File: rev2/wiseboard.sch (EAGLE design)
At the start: 75 parts, among them IC2 LM358MX, Q1 IRLML6402TRPBF, Q2 IRLML6402TRPBF, U1 LT1945EMSPBF, U2 BQ24210DQCT, U3 ESP-WROOM-03

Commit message: Connect flash chip, battery voltage, solar cell voltage
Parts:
- removed C16, C9: 2u2F, resistor:C-USC0805
- removed JP4: JUMPER, Sparkfun-Passives:JUMPER-SMT_2_NC_PASTE_NO-SILK
- removed Q2: IRLML6402TRPBF, IRLML6402:IRLML6402TRPBF
- removed R28: 10k, resistor:R-US_R0805
- removed R29: 33k, resistor:R-US_R0805
- added C10: 10uF, resistor:C-USC0805
- added R15, R17, R18: 10K, resistor:R-US_R0805
- R1: value 12k -> 10K
- R16: value 100k -> 10k
- R2: value 47k -> 10k
- renumbered R35 to R16
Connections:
- removed net 15V: U$4.VPOS
- removed net BOOSTENA: R2.1
- removed net CHARGE_EN: JP4.2, U2.!EN
- removed net N$12: R28.2
- removed net N$13: C9.1, D1.C, U2.VBUS
- removed net N$24: U3.TXD
- removed net N$25: U3.RXD
- removed net N$26: R16.1, S3.P, S3.P1, S4.P, S4.P1, S5.P, S5.P1, S6.P, S6.P1, S7.P, S7.P1
- removed net N$3: Q1.G, R1.2, R2.2
- removed net N$32: U3.IO0
- removed net N$44: U3.IO26
- removed net N$50: U3.SENSOR_VP
- removed net N$51: U3.SENSOR_VN
- removed net N$7: D1.A, SOLAR.2, SOLARPIN.2
- removed net VDD: Q2.D
- new net BAT_SENS: R1.1, R15.2, U3.SENSOR_VP
- new net CLK: U$23.CLK, U3.SCK
- new net CS: U$23.CS, U3.SCS
- new net DPAD: R16.1, S3.P, S3.P1, S4.P, S4.P1, S5.P, S5.P1, S6.P, S6.P1, S7.P, S7.P1, U3.IO0
- new net ESP_DI: U$23.DO, U3.SDI
- new net ESP_DO: U$23.DI, U3.SDO
- new net PANEL: C8.2, D1.A, D1.C, R17.2, SOLAR.2, SOLARPIN.2, U2.VBUS
- new net PANEL_SENS: R17.1, R18.2, U3.SENSOR_VN
- new net SUP_CTRL: Q1.G, R2.2, U3.IO26
- net +15V: now also U$4.VPOS
- net +3V3: now also U3.3V3, U3.EN; no longer C16.1, Q2.S
- net GND: now also C10.1, C8.1, R15.1, R18.1, U2.!EN; no longer C16.2, C8.2, C9.2, JP4.1
- net RXD: now also U3.RXD
- net TXD: now also U3.TXD
- net VBAT: now also C10.2, R1.2, R2.1; no longer C8.1, R1.1
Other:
- note added: "Check to see if these are need."
- moved on the sheet: C8, R1, R2

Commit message: first run through of ERC
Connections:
- removed net N$41: U3.IO21
- new net N$3: C8.2, D1.C, U2.VBUS
- net PANEL: no longer C8.2, D1.C, U2.VBUS
- net SPH: now also U3.IO21
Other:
- note added: "Screen Connector"
- note removed: "Check to see if these are need."
- note removed: "Shift Registers and Screen Connector"
- moved on the sheet: BAT_CON, BAT_PIN, C10, C8, CHRG/LBO, D1, D2, DONE, POWERGOOD, R1, R10, R13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

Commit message: Semi-Final Schematic
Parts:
- removed R16, R32: 10k, resistor:R-US_R0805
- removed R30: 1K, resistor:R-US_R0805
- removed R31: 2k, resistor:R-US_R0805
- removed R33: 12k, resistor:R-US_R0805
- removed R34: 33k, resistor:R-US_R0805
- removed S1, S2, S3, S4, S5, S6, S7: (no value), switch-omron:10-XX
- removed U$23: W25Q32JVSSIQ, WISE:W25Q32JVSSIQ
- added IC5: W25Q, WISE:W25Q32JVSSIQ
- added SW1, SW2: SPST_TACT-KMR2, adafruit:SPST_TACT-KMR2
- IC1: value LT1945EMSPBF -> LT1945
- IC2: value LM358MX -> LM358
- IC3: value 497-7303-1-ND -> L79L15
- IC4: value 497-7278-1-ND -> L78L15
- renumbered U$2 to IC4, U$3 to IC3, U1 to IC1
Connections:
- removed net CS: U$23.CS, U3.SCS
- removed net DPAD: R16.1, S3.P, S3.P1, S4.P, S4.P1, S5.P, S5.P1, S6.P, S6.P1, S7.P, S7.P1, U3.IO0
- removed net N$27: R30.1, S3.S, S3.S1
- removed net N$29: R31.1, S4.S, S4.S1
- removed net N$31: R32.1, S5.S, S5.S1
- removed net N$33: R33.1, S6.S, S6.S1
- removed net N$35: R34.1, S7.S, S7.S1
- new net IC5: IC5.CS, U3.SCS
- new net N$7: U3.IO0
- net +3V3: now also IC5.VCC, IC5.WP; no longer R30.2, R31.2, R32.2, R33.2, R34.2, U$23.VCC, U$23.WP
- net -20V: now also IC3.VIN@3, IC3.VIN@6, IC3.VIN@7
- net CLK: now also IC5.CLK; no longer U$23.CLK
- net ESP_DI: now also IC5.DO; no longer U$23.DO
- net ESP_DO: now also IC5.DI; no longer U$23.DI
- net GND: now also IC5.GND, SW1.P, SW1.P1, SW2.P, SW2.P1; no longer R16.2, S1.P, S1.P1, S2.P, S2.P1, U$23.GND
- net GPIO0: now also SW1.S, SW1.S1; no longer S1.S, S1.S1
- net RESET: now also SW2.S, SW2.S1; no longer S2.S, S2.S1
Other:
- note removed: "Button Array and Battery Monitor"
- moved on the sheet: C7, D2, D3, IC2A, JP1, R22, R9, VR1

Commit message: Add edge connectors to lbr, Prelim PCB layout, Consolidation, Fix mistakes
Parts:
- removed BAT_CON: (no value), adafruit:JST_2PIN-SMT-RA
- removed BAT_PIN, SOLARPIN: (no value), pinhead:PINHD-1X2
- removed C7: 100nF, resistor:C-USC0805
- removed JP1: PROG_HEADER, pinhead:PINHD-1X4
- removed R11, R12: 10k, resistor:R-US_R0805
- removed SOLAR: 455-1749-1-ND, adafruit:JST_2PIN-SMT-RA
- added J1: BAT_CON, WISE:EDGE_CON_22PIN
- added J2: SOL_CON, WISE:EDGE_CON_22PIN
- added J3: PROG_HEADER, WISE:EDGE_CON_4
- BOOT: value GREEN -> LED1
- C1, C3, C6: value 100nF -> 1uF
- C2: value 2u2F -> 1uF
- C4: value 100pF -> 10uF
- C5: value 4.7pF -> 10uF
- CHRG/LBO: value ORANGE -> LED3
- DONE: value GREEN -> LED4
- IC8: value AP2112K-3.3TRG1DICT-ND -> IC6
- POWERGOOD: value BLUE -> LED2
- Q1: value IRLML6402TRPBF -> IRLM
- R4, R7: value 33k -> 39k
- renumbered U$14 to IC8, U$6 to D4, U$7 to D5, U$8 to D6, U2 to IC9
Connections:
- net +15V: no longer IC2P.V+
- net -15V: no longer IC2P.V-
- net GND: now also J1.1, J2.1, J3.4; no longer BAT_CON.1, BAT_PIN.2, C7.2, JP1.4, R11.1, R12.1, SOLAR.1, SOLARPIN.1
- net NEGEN: no longer R11.2
- net PANEL: now also J2.2; no longer SOLAR.2, SOLARPIN.2
- net POSEN: no longer R12.2
- net RXD_5V: now also J3.2; no longer JP1.2
- net TXD: now also J3.1; no longer JP1.1
- net VBAT: now also J1.2; no longer BAT_CON.2, BAT_PIN.1
- net VCC: now also J3.3; no longer JP1.3
- net VCOMMON: no longer C7.1

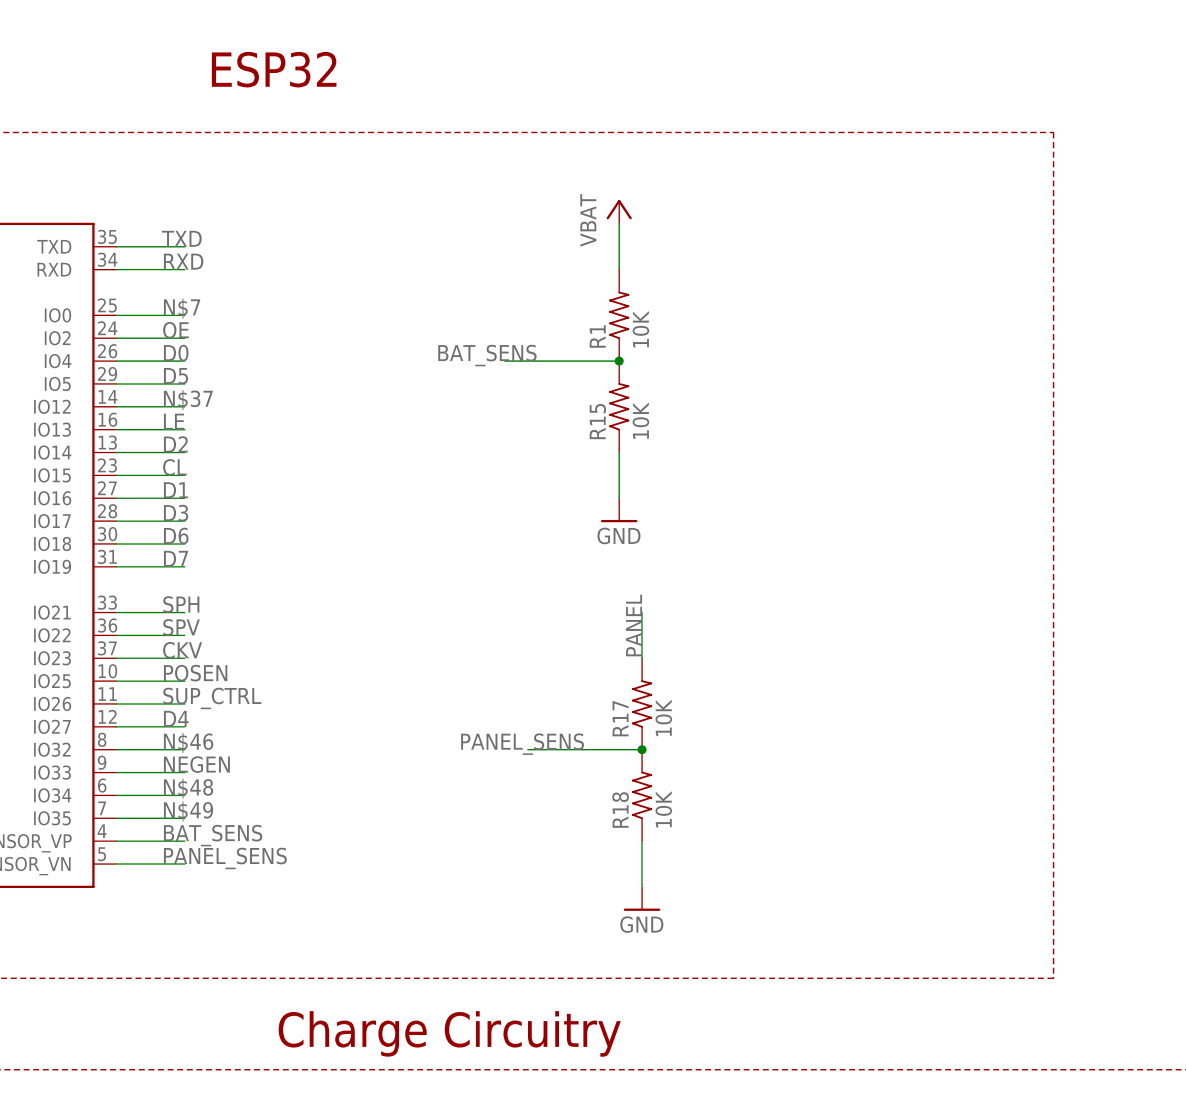
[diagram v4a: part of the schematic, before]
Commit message: Add button header, 2nd revision of pcb layout, mess up a bunch of save files
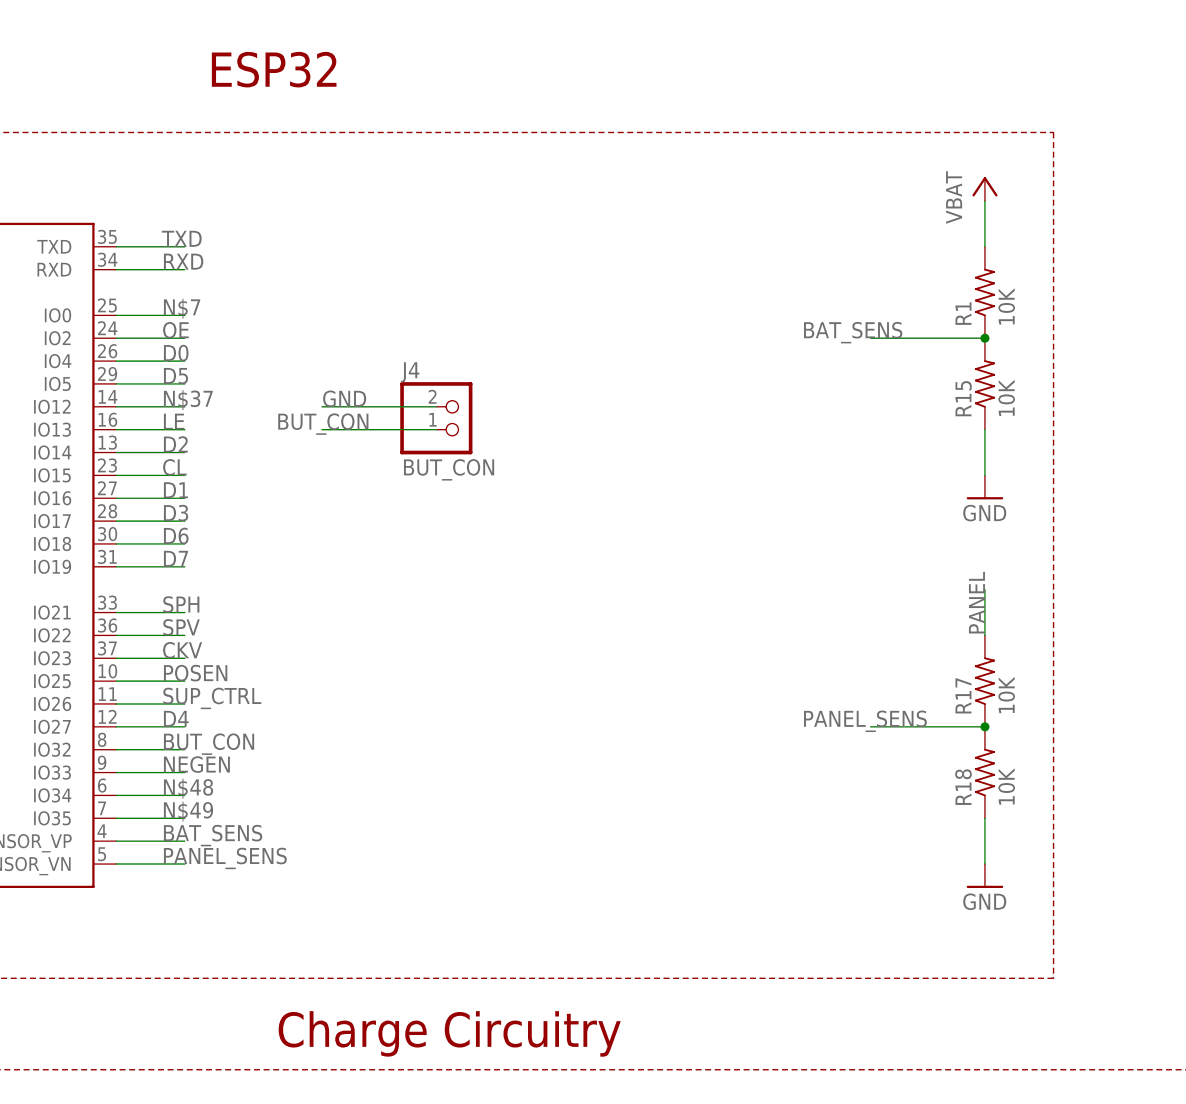
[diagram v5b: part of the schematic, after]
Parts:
- added J4: BUT_CON, WISE:EDGE_CON_22PIN
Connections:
- removed net N$46: U3.IO32
- new net BUT_CON: J4.2, U3.IO32
- net GND: now also J4.1
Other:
- moved on the sheet: R1, R15, R17, R18
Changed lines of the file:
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@@
 <part name="J2" library="WISE" deviceset="EDGE_CON_2" device="2PIN" value="SOL_CON"/>
 <part name="J3" library="WISE" deviceset="EDGE_CON_4" device="" value="PROG_HEADER"/>
+<part name="J4" library="WISE" deviceset="EDGE_CON_2" device="2PIN" value="BUT_CON"/>
 </parts>
 <sheets>
@@
 <instance part="R2" gate="G$1" x="-365.76" y="-33.02" rot="R270"/>
 <instance part="+3V3" gate="G$1" x="93.98" y="12.7" rot="R90"/>
-<instance part="R1" gate="G$1" x="195.58" y="7.62" rot="R90"/>
-<instance part="R15" gate="G$1" x="195.58" y="-2.54" rot="R90"/>
-<instance part="U$1" gate="G$1" x="195.58" y="20.32"/>
-<instance part="GND24" gate="1" x="195.58" y="-15.24"/>
+<instance part="R1" gate="G$1" x="236.22" y="10.16" rot="R90"/>
+<instance part="R15" gate="G$1" x="236.22" y="0" rot="R90"/>
+<instance part="U$1" gate="G$1" x="236.22" y="22.86"/>
+<instance part="GND24" gate="1" x="236.22" y="-12.7"/>
 <instance part="C10" gate="G$1" x="236.22" y="-106.68"/>
 <instance part="GND27" gate="1" x="236.22" y="-99.06" rot="R180"/>
 <instance part="C8" gate="G$1" x="132.08" y="-96.52"/>
-<instance part="R17" gate="G$1" x="198.12" y="-35.56" rot="R90"/>
-<instance part="R18" gate="G$1" x="198.12" y="-45.72" rot="R90"/>
-<instance part="GND28" gate="1" x="198.12" y="-58.42"/>
+<instance part="R17" gate="G$1" x="236.22" y="-33.02" rot="R90"/>
+<instance part="R18" gate="G$1" x="236.22" y="-43.18" rot="R90"/>
+<instance part="GND28" gate="1" x="236.22" y="-55.88"/>
 <instance part="SW1" gate="G$1" x="-2.54" y="55.88"/>
 <instance part="SW2" gate="G$1" x="17.78" y="55.88"/>
@@
 <instance part="J2" gate="G$1" x="93.98" y="-111.76" rot="R180"/>
 <instance part="J3" gate="G$1" x="162.56" y="73.66" rot="R180"/>
+<instance part="J4" gate="G$1" x="177.8" y="-2.54"/>
 </instances>
 <busses>
@@
 <pinref part="R15" gate="G$1" pin="1"/>
 <pinref part="GND24" gate="1" pin="GND"/>
-<wire x1="195.58" y1="-12.7" x2="195.58" y2="-7.62" width="0.1524" layer="91"/>
+<wire x1="236.22" y1="-10.16" x2="236.22" y2="-5.08" width="0.1524" layer="91"/>
 </segment>
 <segment>
@@
 <pinref part="R18" gate="G$1" pin="1"/>
 <pinref part="GND28" gate="1" pin="GND"/>
-<wire x1="198.12" y1="-55.88" x2="198.12" y2="-50.8" width="0.1524" layer="91"/>
+<wire x1="236.22" y1="-53.34" x2="236.22" y2="-48.26" width="0.1524" layer="91"/>
+</segment>
+<segment>
+<pinref part="J4" gate="G$1" pin="1"/>
+<wire x1="175.26" y1="-2.54" x2="162.56" y2="-2.54" width="0.1524" layer="91"/>
+<label x="162.56" y="-2.54" size="1.778" layer="95"/>
 </segment>
 </net>
@@
 <segment>
 <pinref part="R17" gate="G$1" pin="2"/>
-<wire x1="198.12" y1="-25.4" x2="198.12" y2="-30.48" width="0.1524" layer="91"/>
-<label x="198.12" y="-30.48" size="1.778" layer="95" rot="R90"/>
+<wire x1="236.22" y1="-22.86" x2="236.22" y2="-27.94" width="0.1524" layer="91"/>
+<label x="236.22" y="-27.94" size="1.778" layer="95" rot="R90"/>
 </segment>
 </net>
@@
 <pinref part="R1" gate="G$1" pin="2"/>
 <pinref part="U$1" gate="G$1" pin="VBAT"/>
-<wire x1="195.58" y1="17.78" x2="195.58" y2="12.7" width="0.1524" layer="91"/>
+<wire x1="236.22" y1="20.32" x2="236.22" y2="15.24" width="0.1524" layer="91"/>
 </segment>
 <segment>
@@
 </segment>
 </net>
-<net name="N$46" class="0">
+<net name="BUT_CON" class="0">
 <segment>
 <pinref part="U3" gate="G$1" pin="IO32"/>
@@
 <label x="144.78" y="-40.64" size="1.778" layer="95"/>
 </segment>
+<segment>
+<pinref part="J4" gate="G$1" pin="2"/>
+<wire x1="175.26" y1="-5.08" x2="162.56" y2="-5.08" width="0.1524" layer="91"/>
+<label x="157.48" y="-5.08" size="1.778" layer="95"/>
+</segment>
 </net>
 <net name="N$48" class="0">
@@
 <net name="BAT_SENS" class="0">
 <segment>
-<wire x1="182.88" y1="2.54" x2="195.58" y2="2.54" width="0.1524" layer="91"/>
+<wire x1="223.52" y1="5.08" x2="236.22" y2="5.08" width="0.1524" layer="91"/>
 <pinref part="R1" gate="G$1" pin="1"/>
 <pinref part="R15" gate="G$1" pin="2"/>
-<junction x="195.58" y="2.54"/>
-<label x="175.26" y="2.54" size="1.778" layer="95"/>
+<junction x="236.22" y="5.08"/>
+<label x="215.9" y="5.08" size="1.778" layer="95"/>
 </segment>
 <segment>
@@
 </segment>
 <segment>
-<wire x1="185.42" y1="-40.64" x2="198.12" y2="-40.64" width="0.1524" layer="91"/>
+<wire x1="223.52" y1="-38.1" x2="236.22" y2="-38.1" width="0.1524" layer="91"/>
 <pinref part="R17" gate="G$1" pin="1"/>
 <pinref part="R18" gate="G$1" pin="2"/>
-<junction x="198.12" y="-40.64"/>
-<label x="177.8" y="-40.64" size="1.778" layer="95"/>
-</segment>
-</net>
+<junction x="236.22" y="-38.1"/>
+<label x="215.9" y="-38.1" size="1.778" layer="95"/>
+</segment>
+</net>

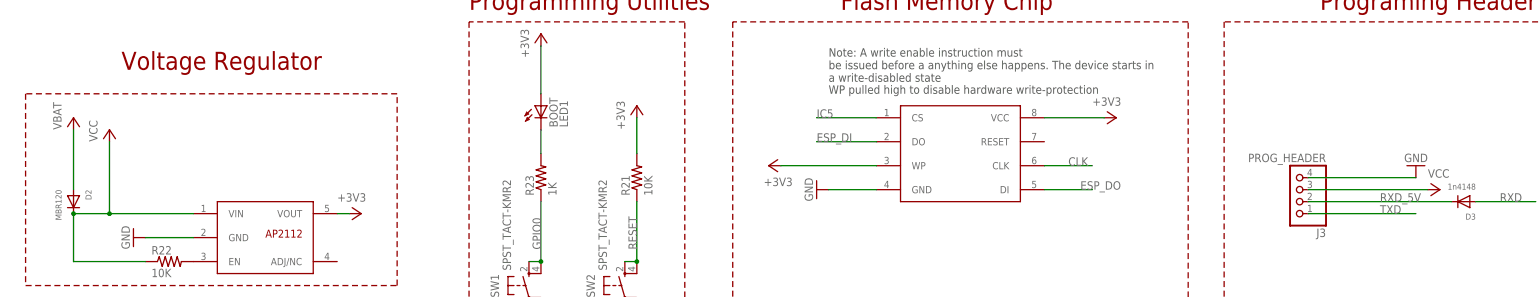
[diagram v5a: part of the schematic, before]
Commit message: fix file troubles, semi finalize layout, fix component labels
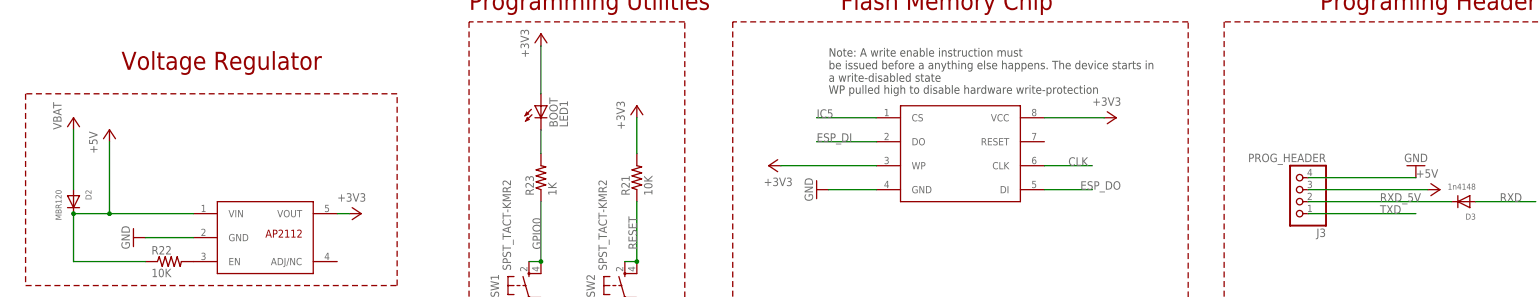
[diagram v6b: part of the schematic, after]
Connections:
- net VCC renamed +5V
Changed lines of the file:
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@@
 <part name="CHRG/LBO" library="adafruit" deviceset="LED" device="CHIP-LED0805" value="LED3"/>
 <part name="GND25" library="supply1" library_urn="urn:adsk.eagle:library:371" deviceset="GND" device=""/>
-<part name="P+10" library="supply1" library_urn="urn:adsk.eagle:library:371" deviceset="VCC" device=""/>
 <part name="D2" library="adafruit" deviceset="DIODE" device="SOD-123" value="MBR120"/>
 <part name="GND32" library="supply1" library_urn="urn:adsk.eagle:library:371" deviceset="GND" device=""/>
@@
 <part name="R10" library="resistor" library_urn="urn:adsk.eagle:library:348" deviceset="R-US_" device="R0805" value="1K"/>
 <part name="GND15" library="supply1" library_urn="urn:adsk.eagle:library:371" deviceset="GND" device=""/>
-<part name="P+2" library="supply1" library_urn="urn:adsk.eagle:library:371" deviceset="VCC" device=""/>
 <part name="IC5" library="WISE" deviceset="W25Q32JVSSIQ" device="" value="W25Q"/>
 <part name="GND20" library="supply1" library_urn="urn:adsk.eagle:library:371" deviceset="GND" device=""/>
@@
 <part name="J3" library="WISE" deviceset="EDGE_CON_4" device="" value="PROG_HEADER"/>
 <part name="J4" library="WISE" deviceset="EDGE_CON_2" device="2PIN" value="BUT_CON"/>
+<part name="P+1" library="supply1" library_urn="urn:adsk.eagle:library:371" deviceset="+5V" device=""/>
+<part name="P+3" library="supply1" library_urn="urn:adsk.eagle:library:371" deviceset="+5V" device=""/>
 </parts>
 <sheets>
@@
 <instance part="CHRG/LBO" gate="G$1" x="248.92" y="-137.16" rot="R180"/>
 <instance part="GND25" gate="1" x="185.42" y="81.28" rot="R180"/>
-<instance part="P+10" gate="VCC" x="190.5" y="76.2" rot="R270"/>
 <instance part="D2" gate="G$1" x="-99.06" y="73.66" rot="R270"/>
 <instance part="GND32" gate="1" x="-86.36" y="66.04" rot="R270"/>
@@
 <instance part="R10" gate="G$1" x="220.98" y="-129.54" rot="R90"/>
 <instance part="GND15" gate="1" x="236.22" y="-139.7"/>
-<instance part="P+2" gate="VCC" x="-91.44" y="88.9"/>
 <instance part="IC5" gate="G$1" x="88.9" y="83.82"/>
 <instance part="GND20" gate="1" x="58.42" y="76.2" rot="R270"/>
@@
 <instance part="J3" gate="G$1" x="162.56" y="73.66" rot="R180"/>
 <instance part="J4" gate="G$1" x="177.8" y="-2.54"/>
+<instance part="P+1" gate="1" x="-91.44" y="88.9"/>
+<instance part="P+3" gate="1" x="190.5" y="76.2" rot="R270"/>
 </instances>
 <busses>
@@
 <wire x1="175.26" y1="-2.54" x2="162.56" y2="-2.54" width="0.1524" layer="91"/>
 <label x="162.56" y="-2.54" size="1.778" layer="95"/>
-</segment>
-</net>
-<net name="VCC" class="0">
-<segment>
-<wire x1="162.56" y1="76.2" x2="187.96" y2="76.2" width="0.1524" layer="91"/>
-<pinref part="P+10" gate="VCC" pin="VCC"/>
-<pinref part="J3" gate="G$1" pin="3"/>
-</segment>
-<segment>
-<pinref part="IC8" gate="G$1" pin="VIN"/>
-<wire x1="-73.66" y1="71.12" x2="-91.44" y2="71.12" width="0.1524" layer="91"/>
-<wire x1="-91.44" y1="71.12" x2="-99.06" y2="71.12" width="0.1524" layer="91"/>
-<wire x1="-99.06" y1="71.12" x2="-99.06" y2="60.96" width="0.1524" layer="91"/>
-<pinref part="D2" gate="G$1" pin="C"/>
-<junction x="-99.06" y="71.12"/>
-<pinref part="R22" gate="G$1" pin="1"/>
-<wire x1="-99.06" y1="60.96" x2="-83.82" y2="60.96" width="0.1524" layer="91"/>
-<pinref part="P+2" gate="VCC" pin="VCC"/>
-<wire x1="-91.44" y1="86.36" x2="-91.44" y2="71.12" width="0.1524" layer="91"/>
-<junction x="-91.44" y="71.12"/>
 </segment>
 </net>
@@
 </segment>
 </net>
+<net name="+5V" class="0">
+<segment>
+<wire x1="162.56" y1="76.2" x2="187.96" y2="76.2" width="0.1524" layer="91"/>
+<pinref part="J3" gate="G$1" pin="3"/>
+<pinref part="P+3" gate="1" pin="+5V"/>
+</segment>
+<segment>
+<pinref part="IC8" gate="G$1" pin="VIN"/>
+<wire x1="-73.66" y1="71.12" x2="-91.44" y2="71.12" width="0.1524" layer="91"/>
+<wire x1="-91.44" y1="71.12" x2="-99.06" y2="71.12" width="0.1524" layer="91"/>
+<wire x1="-99.06" y1="71.12" x2="-99.06" y2="60.96" width="0.1524" layer="91"/>
+<pinref part="D2" gate="G$1" pin="C"/>
+<junction x="-99.06" y="71.12"/>
+<pinref part="R22" gate="G$1" pin="1"/>
+<wire x1="-99.06" y1="60.96" x2="-83.82" y2="60.96" width="0.1524" layer="91"/>
+<wire x1="-91.44" y1="86.36" x2="-91.44" y2="71.12" width="0.1524" layer="91"/>
+<junction x="-91.44" y="71.12"/>
+<pinref part="P+1" gate="1" pin="+5V"/>
+</segment>
+</net>
